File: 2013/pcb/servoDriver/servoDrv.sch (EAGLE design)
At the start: 9 parts, among them X1 22-23-2041

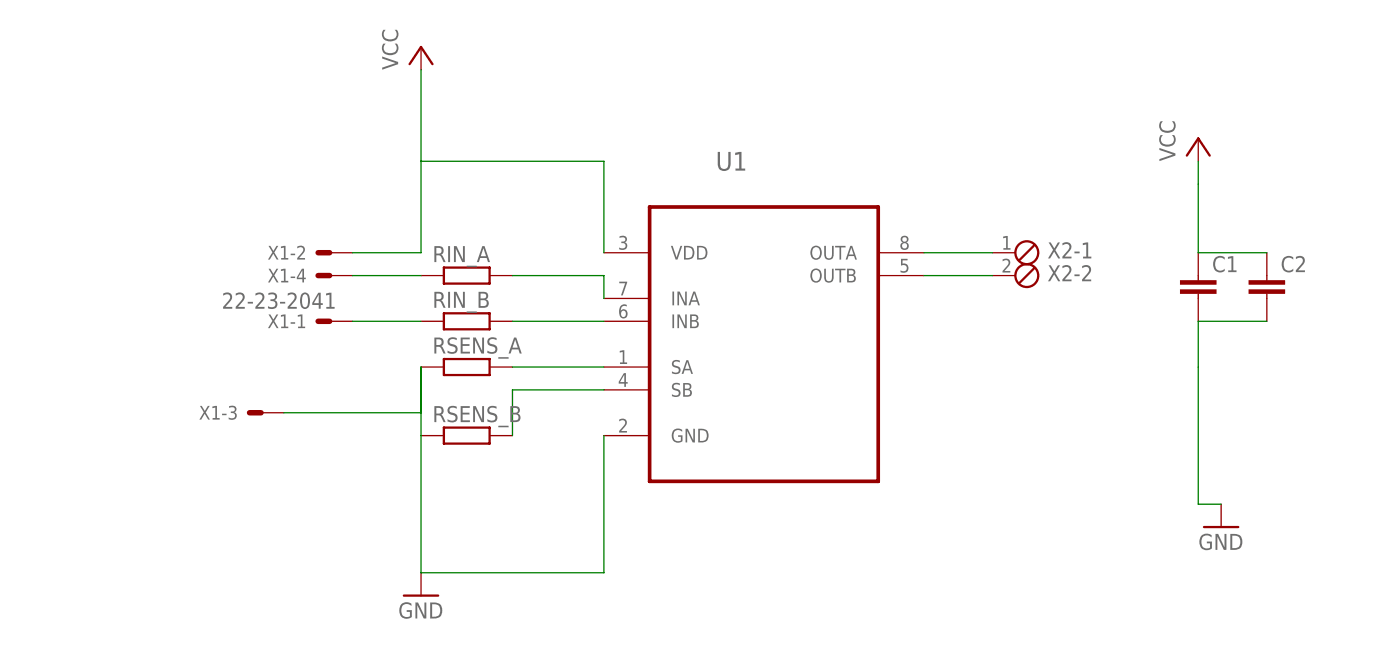
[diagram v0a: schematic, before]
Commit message: servodriverin skemaa muutettu, lisätty tvs:t inputteihin ja poistettu sense-vastukset. Myös puuttuvat viat lisätty.
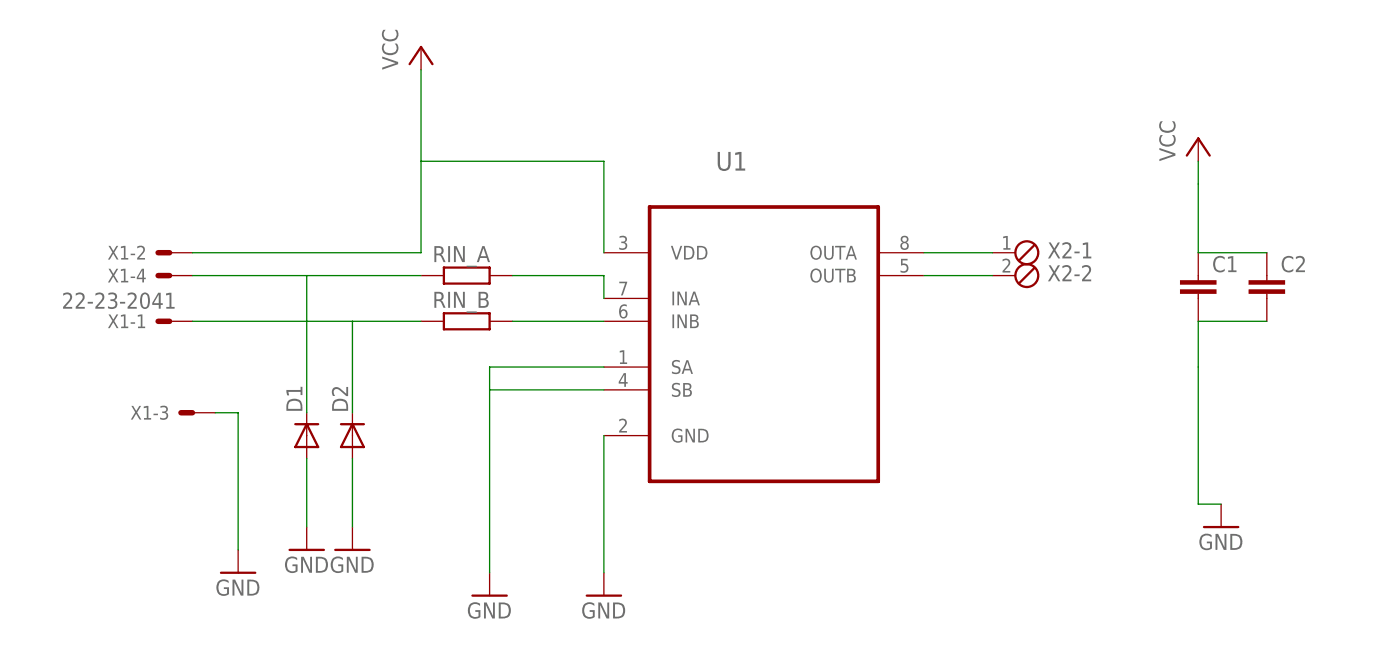
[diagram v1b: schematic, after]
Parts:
- removed RSENS_A, RSENS_B: (no value), resistor:R-EU_R1206
- added D1, D2: (no value), diode:DIODE-SOD123
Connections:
- removed net N$3: RSENS_A.2, U1.SA
- removed net N$4: RSENS_B.2, U1.SB
- net GND: now also D1.A, D2.A, U1.SA, U1.SB; no longer RSENS_A.1, RSENS_B.1
- net N$5: now also D1.C
- net N$8: now also D2.C
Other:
- moved on the sheet: X1-1, X1-2, X1-3, X1-4
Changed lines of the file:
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@@
 <part name="X1" library="con-molex" deviceset="22-23-2041" device=""/>
 <part name="X2" library="con-phoenix-254" deviceset="MPT2" device=""/>
-<part name="RSENS_A" library="resistor" deviceset="R-EU_" device="R1206"/>
-<part name="RSENS_B" library="resistor" deviceset="R-EU_" device="R1206"/>
 <part name="RIN_A" library="resistor" deviceset="R-EU_" device="R0805"/>
 <part name="RIN_B" library="resistor" deviceset="R-EU_" device="R0805"/>
@@
 <part name="P+2" library="supply1" deviceset="VCC" device=""/>
 <part name="GND2" library="supply1" deviceset="GND" device=""/>
+<part name="D1" library="diode" deviceset="DIODE-" device="SOD123"/>
+<part name="D2" library="diode" deviceset="DIODE-" device="SOD123"/>
+<part name="GND3" library="supply1" deviceset="GND" device=""/>
+<part name="GND4" library="supply1" deviceset="GND" device=""/>
+<part name="GND5" library="supply1" deviceset="GND" device=""/>
+<part name="GND6" library="supply1" deviceset="GND" device=""/>
 </parts>
 <sheets>
@@
 <instance part="U1" gate="A" x="45.72" y="60.96"/>
 <instance part="P+1" gate="VCC" x="7.62" y="91.44"/>
-<instance part="GND1" gate="1" x="7.62" y="30.48"/>
-<instance part="X1" gate="-1" x="-2.54" y="60.96" rot="MR0"/>
-<instance part="X1" gate="-2" x="-2.54" y="68.58" rot="MR0"/>
-<instance part="X1" gate="-3" x="-10.16" y="50.8" rot="MR0"/>
-<instance part="X1" gate="-4" x="-2.54" y="66.04" rot="MR0"/>
+<instance part="GND1" gate="1" x="-12.7" y="33.02"/>
+<instance part="X1" gate="-1" x="-20.32" y="60.96" rot="MR0"/>
+<instance part="X1" gate="-2" x="-20.32" y="68.58" rot="MR0"/>
+<instance part="X1" gate="-3" x="-17.78" y="50.8" rot="MR0"/>
+<instance part="X1" gate="-4" x="-20.32" y="66.04" rot="MR0"/>
 <instance part="X2" gate="-1" x="73.66" y="68.58"/>
 <instance part="X2" gate="-2" x="73.66" y="66.04"/>
-<instance part="RSENS_A" gate="G$1" x="12.7" y="55.88"/>
-<instance part="RSENS_B" gate="G$1" x="12.7" y="48.26"/>
 <instance part="RIN_A" gate="G$1" x="12.7" y="66.04"/>
 <instance part="RIN_B" gate="G$1" x="12.7" y="60.96"/>
@@
 <instance part="P+2" gate="VCC" x="93.98" y="81.28"/>
 <instance part="GND2" gate="1" x="96.52" y="38.1"/>
+<instance part="D1" gate="G$1" x="-5.08" y="48.26" rot="R90"/>
+<instance part="D2" gate="G$1" x="0" y="48.26" rot="R90"/>
+<instance part="GND3" gate="1" x="27.94" y="30.48"/>
+<instance part="GND4" gate="1" x="15.24" y="30.48"/>
+<instance part="GND5" gate="1" x="-5.08" y="35.56"/>
+<instance part="GND6" gate="1" x="0" y="35.56"/>
 </instances>
 <busses>
@@
 <wire x1="27.94" y1="78.74" x2="7.62" y2="78.74" width="0.1524" layer="91"/>
 <pinref part="X1" gate="-2" pin="S"/>
-<wire x1="0" y1="68.58" x2="7.62" y2="68.58" width="0.1524" layer="91"/>
+<wire x1="-17.78" y1="68.58" x2="7.62" y2="68.58" width="0.1524" layer="91"/>
 </segment>
 <segment>
@@
 <segment>
 <pinref part="GND1" gate="1" pin="GND"/>
-<pinref part="U1" gate="A" pin="GND"/>
-<wire x1="7.62" y1="33.02" x2="27.94" y2="33.02" width="0.1524" layer="91"/>
-<wire x1="27.94" y1="33.02" x2="27.94" y2="48.26" width="0.1524" layer="91"/>
-<pinref part="RSENS_B" gate="G$1" pin="1"/>
-<wire x1="7.62" y1="48.26" x2="7.62" y2="33.02" width="0.1524" layer="91"/>
-<pinref part="RSENS_A" gate="G$1" pin="1"/>
-<wire x1="7.62" y1="55.88" x2="7.62" y2="48.26" width="0.1524" layer="91"/>
+<wire x1="-12.7" y1="50.8" x2="-12.7" y2="35.56" width="0.1524" layer="91"/>
 <pinref part="X1" gate="-3" pin="S"/>
-<wire x1="-7.62" y1="50.8" x2="7.62" y2="50.8" width="0.1524" layer="91"/>
-<wire x1="7.62" y1="50.8" x2="7.62" y2="55.88" width="0.1524" layer="91"/>
+<wire x1="-15.24" y1="50.8" x2="-12.7" y2="50.8" width="0.1524" layer="91"/>
 </segment>
 <segment>
@@
 <wire x1="101.6" y1="60.96" x2="93.98" y2="60.96" width="0.1524" layer="91"/>
 <wire x1="93.98" y1="60.96" x2="93.98" y2="55.88" width="0.1524" layer="91"/>
+</segment>
+<segment>
+<pinref part="U1" gate="A" pin="SA"/>
+<wire x1="15.24" y1="55.88" x2="27.94" y2="55.88" width="0.1524" layer="91"/>
+<pinref part="GND4" gate="1" pin="GND"/>
+<wire x1="15.24" y1="55.88" x2="15.24" y2="53.34" width="0.1524" layer="91"/>
+<pinref part="U1" gate="A" pin="SB"/>
+<wire x1="15.24" y1="53.34" x2="15.24" y2="33.02" width="0.1524" layer="91"/>
+<wire x1="27.94" y1="53.34" x2="15.24" y2="53.34" width="0.1524" layer="91"/>
+</segment>
+<segment>
+<pinref part="U1" gate="A" pin="GND"/>
+<pinref part="GND3" gate="1" pin="GND"/>
+<wire x1="27.94" y1="48.26" x2="27.94" y2="33.02" width="0.1524" layer="91"/>
+</segment>
+<segment>
+<pinref part="D1" gate="G$1" pin="A"/>
+<pinref part="GND5" gate="1" pin="GND"/>
+<wire x1="-5.08" y1="45.72" x2="-5.08" y2="38.1" width="0.1524" layer="91"/>
+</segment>
+<segment>
+<pinref part="GND6" gate="1" pin="GND"/>
+<pinref part="D2" gate="G$1" pin="A"/>
+<wire x1="0" y1="38.1" x2="0" y2="45.72" width="0.1524" layer="91"/>
 </segment>
 </net>
@@
 <pinref part="X2" gate="-2" pin="1"/>
 <wire x1="63.5" y1="66.04" x2="71.12" y2="66.04" width="0.1524" layer="91"/>
-</segment>
-</net>
-<net name="N$3" class="0">
-<segment>
-<pinref part="RSENS_A" gate="G$1" pin="2"/>
-<pinref part="U1" gate="A" pin="SA"/>
-<wire x1="17.78" y1="55.88" x2="27.94" y2="55.88" width="0.1524" layer="91"/>
-</segment>
-</net>
-<net name="N$4" class="0">
-<segment>
-<pinref part="U1" gate="A" pin="SB"/>
-<pinref part="RSENS_B" gate="G$1" pin="2"/>
-<wire x1="27.94" y1="53.34" x2="17.78" y2="53.34" width="0.1524" layer="91"/>
-<wire x1="17.78" y1="53.34" x2="17.78" y2="48.26" width="0.1524" layer="91"/>
 </segment>
 </net>
@@
 <pinref part="X1" gate="-1" pin="S"/>
 <pinref part="RIN_B" gate="G$1" pin="1"/>
+<wire x1="-17.78" y1="60.96" x2="0" y2="60.96" width="0.1524" layer="91"/>
+<pinref part="D2" gate="G$1" pin="C"/>
 <wire x1="0" y1="60.96" x2="7.62" y2="60.96" width="0.1524" layer="91"/>
+<wire x1="0" y1="50.8" x2="0" y2="60.96" width="0.1524" layer="91"/>
 </segment>
 </net>
@@
 <pinref part="X1" gate="-4" pin="S"/>
 <pinref part="RIN_A" gate="G$1" pin="1"/>
-<wire x1="0" y1="66.04" x2="7.62" y2="66.04" width="0.1524" layer="91"/>
+<wire x1="-17.78" y1="66.04" x2="-5.08" y2="66.04" width="0.1524" layer="91"/>
+<pinref part="D1" gate="G$1" pin="C"/>
+<wire x1="-5.08" y1="66.04" x2="7.62" y2="66.04" width="0.1524" layer="91"/>
+<wire x1="-5.08" y1="50.8" x2="-5.08" y2="66.04" width="0.1524" layer="91"/>
 </segment>
 </net>

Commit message: Lisää muutoksia servodriveriin, board outline lisätty.
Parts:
- X2: device con-phoenix-254:MPT2 -> con-ptr500:AK500/2
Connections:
- net N$1: now also X2-1.KL; no longer X2-1.1
- net N$2: now also X2-2.KL; no longer X2-2.1
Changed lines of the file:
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@@
 <grid distance="0.1" unitdist="inch" unit="inch" style="lines" multiple="1" display="no" altdistance="0.01" altunitdist="inch" altunit="inch"/>
 <layers>
-<layer number="1" name="Top" color="4" fill="1" visible="no" active="no"/>
-<layer number="16" name="Bottom" color="1" fill="1" visible="no" active="no"/>
-<layer number="17" name="Pads" color="2" fill="1" visible="no" active="no"/>
-<layer number="18" name="Vias" color="2" fill="1" visible="no" active="no"/>
-<layer number="19" name="Unrouted" color="6" fill="1" visible="no" active="no"/>
-<layer number="20" name="Dimension" color="15" fill="1" visible="no" active="no"/>
-<layer number="21" name="tPlace" color="7" fill="1" visible="no" active="no"/>
-<layer number="22" name="bPlace" color="7" fill="1" visible="no" active="no"/>
-<layer number="23" name="tOrigins" color="15" fill="1" visible="no" active="no"/>
-<layer number="24" name="bOrigins" color="15" fill="1" visible="no" active="no"/>
-<layer number="25" name="tNames" color="7" fill="1" visible="no" active="no"/>
-<layer number="26" name="bNames" color="7" fill="1" visible="no" active="no"/>
-<layer number="27" name="tValues" color="7" fill="1" visible="no" active="no"/>
-<layer number="28" name="bValues" color="7" fill="1" visible="no" active="no"/>
+<layer number="1" name="Top" color="4" fill="1" visible="yes" active="no"/>
+<layer number="16" name="Bottom" color="1" fill="1" visible="yes" active="no"/>
+<layer number="17" name="Pads" color="2" fill="1" visible="yes" active="no"/>
+<layer number="18" name="Vias" color="2" fill="1" visible="yes" active="no"/>
+<layer number="19" name="Unrouted" color="6" fill="1" visible="yes" active="no"/>
+<layer number="20" name="Dimension" color="15" fill="1" visible="yes" active="no"/>
+<layer number="21" name="tPlace" color="7" fill="1" visible="yes" active="no"/>
+<layer number="22" name="bPlace" color="7" fill="1" visible="yes" active="no"/>
+<layer number="23" name="tOrigins" color="15" fill="1" visible="yes" active="no"/>
+<layer number="24" name="bOrigins" color="15" fill="1" visible="yes" active="no"/>
+<layer number="25" name="tNames" color="7" fill="1" visible="yes" active="no"/>
+<layer number="26" name="bNames" color="7" fill="1" visible="yes" active="no"/>
+<layer number="27" name="tValues" color="7" fill="1" visible="yes" active="no"/>
+<layer number="28" name="bValues" color="7" fill="1" visible="yes" active="no"/>
 <layer number="29" name="tStop" color="7" fill="3" visible="no" active="no"/>
 <layer number="30" name="bStop" color="7" fill="6" visible="no" active="no"/>
@@
 <layer number="35" name="tGlue" color="7" fill="4" visible="no" active="no"/>
 <layer number="36" name="bGlue" color="7" fill="5" visible="no" active="no"/>
-<layer number="37" name="tTest" color="7" fill="1" visible="no" active="no"/>
-<layer number="38" name="bTest" color="7" fill="1" visible="no" active="no"/>
+<layer number="37" name="tTest" color="7" fill="1" visible="yes" active="no"/>
+<layer number="38" name="bTest" color="7" fill="1" visible="yes" active="no"/>
 <layer number="39" name="tKeepout" color="4" fill="11" visible="no" active="no"/>
 <layer number="40" name="bKeepout" color="1" fill="11" visible="no" active="no"/>
@@
 <layer number="44" name="Drills" color="7" fill="1" visible="no" active="no"/>
 <layer number="45" name="Holes" color="7" fill="1" visible="no" active="no"/>
-<layer number="46" name="Milling" color="3" fill="1" visible="no" active="no"/>
-<layer number="47" name="Measures" color="7" fill="1" visible="no" active="no"/>
-<layer number="48" name="Document" color="7" fill="1" visible="no" active="no"/>
-<layer number="49" name="Reference" color="7" fill="1" visible="no" active="no"/>
-<layer number="51" name="tDocu" color="7" fill="1" visible="no" active="no"/>
-<layer number="52" name="bDocu" color="7" fill="1" visible="no" active="no"/>
+<layer number="46" name="Milling" color="3" fill="1" visible="yes" active="no"/>
+<layer number="47" name="Measures" color="7" fill="1" visible="yes" active="no"/>
+<layer number="48" name="Document" color="7" fill="1" visible="yes" active="no"/>
+<layer number="49" name="Reference" color="7" fill="1" visible="yes" active="no"/>
+<layer number="51" name="tDocu" color="7" fill="1" visible="yes" active="no"/>
+<layer number="52" name="bDocu" color="7" fill="1" visible="yes" active="no"/>
 <layer number="91" name="Nets" color="2" fill="1" visible="yes" active="yes"/>
 <layer number="92" name="Busses" color="1" fill="1" visible="yes" active="yes"/>
@@
 <part name="GND1" library="supply1" deviceset="GND" device=""/>
 <part name="X1" library="con-molex" deviceset="22-23-2041" device=""/>
-<part name="X2" library="con-phoenix-254" deviceset="MPT2" device=""/>
+<part name="X2" library="con-ptr500" deviceset="AK500/2" device=""/>
 <part name="RIN_A" library="resistor" deviceset="R-EU_" device="R0805"/>
 <part name="RIN_B" library="resistor" deviceset="R-EU_" device="R0805"/>
@@
 <instance part="X1" gate="-3" x="-17.78" y="50.8" rot="MR0"/>
 <instance part="X1" gate="-4" x="-20.32" y="66.04" rot="MR0"/>
-<instance part="X2" gate="-1" x="73.66" y="68.58"/>
-<instance part="X2" gate="-2" x="73.66" y="66.04"/>
+<instance part="X2" gate="-1" x="76.2" y="60.96" rot="R90"/>
+<instance part="X2" gate="-2" x="68.58" y="58.42" rot="R90"/>
 <instance part="RIN_A" gate="G$1" x="12.7" y="66.04"/>
 <instance part="RIN_B" gate="G$1" x="12.7" y="60.96"/>
@@
 <segment>
 <pinref part="U1" gate="A" pin="OUTA"/>
-<pinref part="X2" gate="-1" pin="1"/>
-<wire x1="63.5" y1="68.58" x2="71.12" y2="68.58" width="0.1524" layer="91"/>
+<pinref part="X2" gate="-1" pin="KL"/>
+<wire x1="63.5" y1="68.58" x2="76.2" y2="66.04" width="0.1524" layer="91"/>
 </segment>
 </net>
@@
 <segment>
 <pinref part="U1" gate="A" pin="OUTB"/>
-<pinref part="X2" gate="-2" pin="1"/>
-<wire x1="63.5" y1="66.04" x2="71.12" y2="66.04" width="0.1524" layer="91"/>
+<pinref part="X2" gate="-2" pin="KL"/>
+<wire x1="63.5" y1="66.04" x2="68.58" y2="63.5" width="0.1524" layer="91"/>
 </segment>
 </net>

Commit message: viimeisin versio servodriverista
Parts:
- C1: value (none) -> 100n
- C2: value (none) -> 1u
- D1, D2: value (none) -> PTVS6V0S1UR
- RIN_A, RIN_B: value (none) -> 100
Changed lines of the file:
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@@
 <grid distance="0.1" unitdist="inch" unit="inch" style="lines" multiple="1" display="no" altdistance="0.01" altunitdist="inch" altunit="inch"/>
 <layers>
-<layer number="1" name="Top" color="4" fill="1" visible="yes" active="no"/>
-<layer number="16" name="Bottom" color="1" fill="1" visible="yes" active="no"/>
-<layer number="17" name="Pads" color="2" fill="1" visible="yes" active="no"/>
-<layer number="18" name="Vias" color="2" fill="1" visible="yes" active="no"/>
-<layer number="19" name="Unrouted" color="6" fill="1" visible="yes" active="no"/>
-<layer number="20" name="Dimension" color="15" fill="1" visible="yes" active="no"/>
-<layer number="21" name="tPlace" color="7" fill="1" visible="yes" active="no"/>
-<layer number="22" name="bPlace" color="7" fill="1" visible="yes" active="no"/>
-<layer number="23" name="tOrigins" color="15" fill="1" visible="yes" active="no"/>
-<layer number="24" name="bOrigins" color="15" fill="1" visible="yes" active="no"/>
-<layer number="25" name="tNames" color="7" fill="1" visible="yes" active="no"/>
-<layer number="26" name="bNames" color="7" fill="1" visible="yes" active="no"/>
-<layer number="27" name="tValues" color="7" fill="1" visible="yes" active="no"/>
-<layer number="28" name="bValues" color="7" fill="1" visible="yes" active="no"/>
+<layer number="1" name="Top" color="4" fill="1" visible="no" active="no"/>
+<layer number="16" name="Bottom" color="1" fill="1" visible="no" active="no"/>
+<layer number="17" name="Pads" color="2" fill="1" visible="no" active="no"/>
+<layer number="18" name="Vias" color="2" fill="1" visible="no" active="no"/>
+<layer number="19" name="Unrouted" color="6" fill="1" visible="no" active="no"/>
+<layer number="20" name="Dimension" color="15" fill="1" visible="no" active="no"/>
+<layer number="21" name="tPlace" color="7" fill="1" visible="no" active="no"/>
+<layer number="22" name="bPlace" color="7" fill="1" visible="no" active="no"/>
+<layer number="23" name="tOrigins" color="15" fill="1" visible="no" active="no"/>
+<layer number="24" name="bOrigins" color="15" fill="1" visible="no" active="no"/>
+<layer number="25" name="tNames" color="7" fill="1" visible="no" active="no"/>
+<layer number="26" name="bNames" color="7" fill="1" visible="no" active="no"/>
+<layer number="27" name="tValues" color="7" fill="1" visible="no" active="no"/>
+<layer number="28" name="bValues" color="7" fill="1" visible="no" active="no"/>
 <layer number="29" name="tStop" color="7" fill="3" visible="no" active="no"/>
 <layer number="30" name="bStop" color="7" fill="6" visible="no" active="no"/>
@@
 <layer number="35" name="tGlue" color="7" fill="4" visible="no" active="no"/>
 <layer number="36" name="bGlue" color="7" fill="5" visible="no" active="no"/>
-<layer number="37" name="tTest" color="7" fill="1" visible="yes" active="no"/>
-<layer number="38" name="bTest" color="7" fill="1" visible="yes" active="no"/>
+<layer number="37" name="tTest" color="7" fill="1" visible="no" active="no"/>
+<layer number="38" name="bTest" color="7" fill="1" visible="no" active="no"/>
 <layer number="39" name="tKeepout" color="4" fill="11" visible="no" active="no"/>
 <layer number="40" name="bKeepout" color="1" fill="11" visible="no" active="no"/>
@@
 <layer number="44" name="Drills" color="7" fill="1" visible="no" active="no"/>
 <layer number="45" name="Holes" color="7" fill="1" visible="no" active="no"/>
-<layer number="46" name="Milling" color="3" fill="1" visible="yes" active="no"/>
-<layer number="47" name="Measures" color="7" fill="1" visible="yes" active="no"/>
-<layer number="48" name="Document" color="7" fill="1" visible="yes" active="no"/>
-<layer number="49" name="Reference" color="7" fill="1" visible="yes" active="no"/>
-<layer number="51" name="tDocu" color="7" fill="1" visible="yes" active="no"/>
-<layer number="52" name="bDocu" color="7" fill="1" visible="yes" active="no"/>
+<layer number="46" name="Milling" color="3" fill="1" visible="no" active="no"/>
+<layer number="47" name="Measures" color="7" fill="1" visible="no" active="no"/>
+<layer number="48" name="Document" color="7" fill="1" visible="no" active="no"/>
+<layer number="49" name="Reference" color="7" fill="1" visible="no" active="no"/>
+<layer number="51" name="tDocu" color="7" fill="1" visible="no" active="no"/>
+<layer number="52" name="bDocu" color="7" fill="1" visible="no" active="no"/>
 <layer number="91" name="Nets" color="2" fill="1" visible="yes" active="yes"/>
 <layer number="92" name="Busses" color="1" fill="1" visible="yes" active="yes"/>
@@
 <part name="X1" library="con-molex" deviceset="22-23-2041" device=""/>
 <part name="X2" library="con-ptr500" deviceset="AK500/2" device=""/>
-<part name="RIN_A" library="resistor" deviceset="R-EU_" device="R0805"/>
-<part name="RIN_B" library="resistor" deviceset="R-EU_" device="R0805"/>
-<part name="C1" library="resistor" deviceset="C-EU" device="C0805"/>
-<part name="C2" library="resistor" deviceset="C-EU" device="C0805"/>
+<part name="RIN_A" library="resistor" deviceset="R-EU_" device="R0805" value="100"/>
+<part name="RIN_B" library="resistor" deviceset="R-EU_" device="R0805" value="100"/>
+<part name="C1" library="resistor" deviceset="C-EU" device="C0805" value="100n"/>
+<part name="C2" library="resistor" deviceset="C-EU" device="C0805" value="1u"/>
 <part name="P+2" library="supply1" deviceset="VCC" device=""/>
 <part name="GND2" library="supply1" deviceset="GND" device=""/>
-<part name="D1" library="diode" deviceset="DIODE-" device="SOD123"/>
-<part name="D2" library="diode" deviceset="DIODE-" device="SOD123"/>
+<part name="D1" library="diode" deviceset="DIODE-" device="SOD123" value="PTVS6V0S1UR"/>
+<part name="D2" library="diode" deviceset="DIODE-" device="SOD123" value="PTVS6V0S1UR"/>
 <part name="GND3" library="supply1" deviceset="GND" device=""/>
 <part name="GND4" library="supply1" deviceset="GND" device=""/>
